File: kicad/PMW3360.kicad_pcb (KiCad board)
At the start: 2 copper layers, 22 x 34 mm, 12 parts, among them J1 Conn_01x07, U1 PMW3360, U2 TCR2EF19

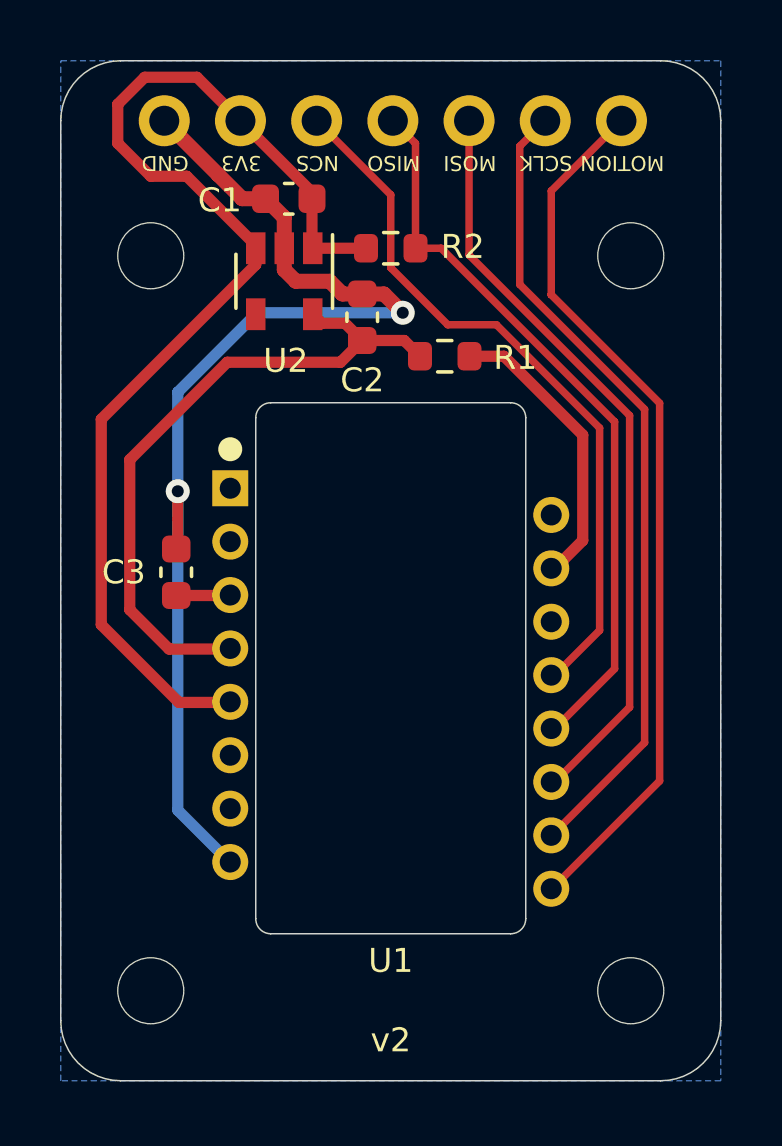
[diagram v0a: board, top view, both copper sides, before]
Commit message: add a reset button
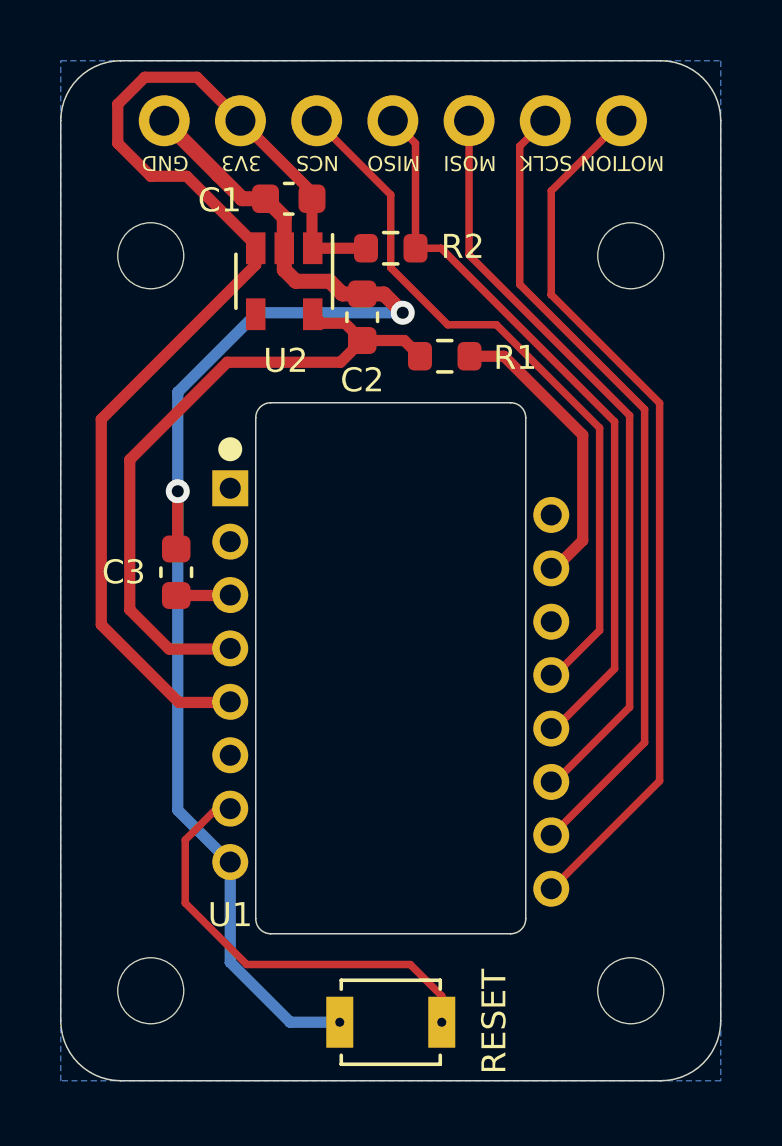
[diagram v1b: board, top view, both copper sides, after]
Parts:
- added sw_reset1: SW_RESET-kbd, mylib:SW_B3U-1000P_reversible, F.Cu at (149.0, 118.0)
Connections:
- U1 pad 1: Net-(U1-Pad1) -> unconnected-(U1-Pad1)
- U1 pad 14: Net-(U1-Pad14) -> unconnected-(U1-Pad14)
- U1 pad 16: Net-(U1-Pad16) -> unconnected-(U1-Pad16)
- U1 pad 2: Net-(U1-Pad2) -> unconnected-(U1-Pad2)
- U1 pad 6: Net-(U1-Pad6) -> unconnected-(U1-Pad6)
- U1 pad 7: Net-(U1-Pad7) -> RESET
- U2 pad 4: Net-(U2-Pad4) -> unconnected-(U2-Pad4)
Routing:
- net RESET: track 0.00 -> 14.7 mm
- net GND: track 38.6 -> 46.3 mm
- net NCS: track 24.5 -> 24.0 mm
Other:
- net class Default removed
- net class power removed
- board text removed: "v2"

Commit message: add 3d model of pmw3360
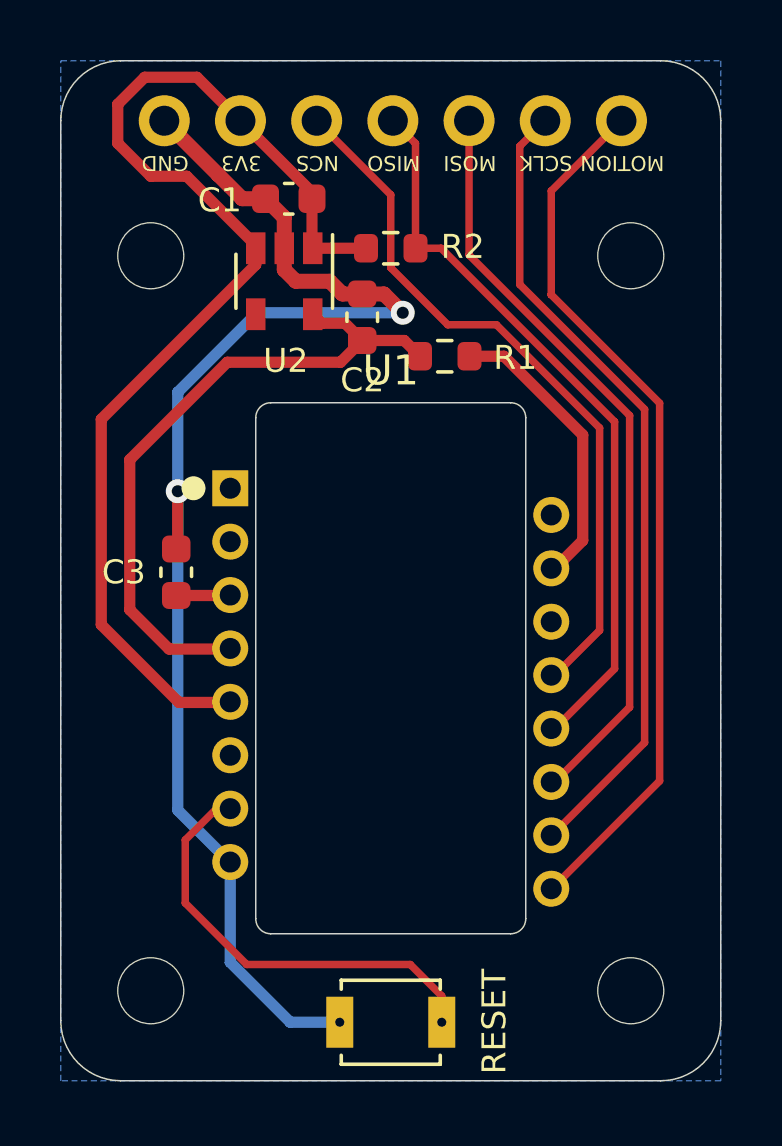
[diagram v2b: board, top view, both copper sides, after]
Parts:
- U1: footprint PMW3360:PMW3360 -> mylib:PMW3360
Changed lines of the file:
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@@
     (pad "" np_thru_hole circle locked (at 0 0) (size 2.2 2.2) (drill 2.2) (layers *.Cu *.Mask))
   )
-  (footprint "PMW3360:PMW3360" (layer "F.Cu")
+  (footprint "mylib:PMW3360" (layer "F.Cu")
     (at 143.65 100.25)
     (property "Sheetfile" "/home/yong/kbd-src/sensors/pmw3360/pmw3360-breakout/kicad/PMW3360.sch")
     (property "Sheetname" "")
     (attr through_hole)
-    (fp_text reference "U1" (at 0 14.225) (layer "F.SilkS")
-      (effects (font (size 0.8 0.8) (thickness 0.15)))
+    (fp_text reference "U1" (at 5.35 -3.925) (layer "F.SilkS")
+      (effects (font (size 1 1) (thickness 0.15)))
     )
     (fp_text value "PMW3360" (at 5.35 13.375) (layer "F.Fab")
       (effects (font (size 1 1) (thickness 0.15)))
     )
-    (fp_circle (center 0 -1.3) (end 0.2 -1.3) (layer "F.SilkS") (width 0.4) (fill none))
+    (fp_circle (center -1.225 0) (end -1.025 0) (layer "F.SilkS") (width 0.4) (fill none))
+    (fp_line (start 9.65 -2.78) (end 9.65 14.48) (layer "Dwgs.User") (width 0.12))
+    (fp_line (start 5.35 4.66) (end 5.35 6.66) (layer "Dwgs.User") (width 0.12))
+    (fp_line (start 1.05 14.48) (end 9.65 14.48) (layer "Dwgs.User") (width 0.12))
+    (fp_line (start 4.35 5.66) (end 6.35 5.66) (layer "Dwgs.User") (width 0.12))
     (fp_line (start 1.05 -2.78) (end 9.65 -2.78) (layer "Dwgs.User") (width 0.12))
-    (fp_line (start 1.05 14.48) (end 9.65 14.48) (layer "Dwgs.User") (width 0.12))
-    (fp_line (start 9.65 -2.78) (end 9.65 14.48) (layer "Dwgs.User") (width 0.12))
-    (fp_line (start 4.35 5.66) (end 6.35 5.66) (layer "Dwgs.User") (width 0.12))
     (fp_line (start 1.05 -2.78) (end 1.05 14.48) (layer "Dwgs.User") (width 0.12))
-    (fp_line (start 5.35 4.66) (end 5.35 6.66) (layer "Dwgs.User") (width 0.12))
+    (fp_line (start 2.975 -5.21) (end 7.725 -5.21) (layer "B.CrtYd") (width 0.05))
     (fp_line (start -4.075 1.84) (end -4.075 8.89) (layer "B.CrtYd") (width 0.05))
-    (fp_line (start 2.975 -5.21) (end 7.725 -5.21) (layer "B.CrtYd") (width 0.05))
     (fp_line (start 14.775 1.84) (end 14.775 8.89) (layer "B.CrtYd") (width 0.05))
     (fp_line (start 2.975 15.94) (end 7.725 15.94) (layer "B.CrtYd") (width 0.05))
+    (fp_arc (start 7.725 -5.21) (mid 12.710103 -3.145103) (end 14.775 1.84) (layer "B.CrtYd") (width 0.05))
     (fp_arc (start 14.775 8.89) (mid 12.710103 13.875103) (end 7.725 15.94) (layer "B.CrtYd") (width 0.05))
+    (fp_arc (start 2.975 15.94) (mid -2.010103 13.875103) (end -4.075 8.89) (layer "B.CrtYd") (width 0.05))
     (fp_arc (start -4.075 1.84) (mid -2.010103 -3.145103) (end 2.975 -5.21) (layer "B.CrtYd") (width 0.05))
-    (fp_arc (start 2.975 15.94) (mid -2.010103 13.875103) (end -4.075 8.89) (layer "B.CrtYd") (width 0.05))
-    (fp_arc (start 7.725 -5.21) (mid 12.710103 -3.145103) (end 14.775 1.84) (layer "B.CrtYd") (width 0.05))
-    (pad "1" thru_hole rect locked (at 0 0) (size 1.2 1.2) (drill 0.7) (layers *.Cu *.Mask)
+    (pad "1" thru_hole rect (at 0 0) (size 1.2 1.2) (drill 0.7) (layers *.Cu *.Mask)
       (net 2 "unconnected-(U1-Pad1)") (pinfunction "NC") (pintype "no_connect"))
-    (pad "2" thru_hole circle locked (at 0 1.78) (size 1.2 1.2) (drill 0.7) (layers *.Cu *.Mask)
+    (pad "2" thru_hole circle (at 0 1.78) (size 1.2 1.2) (drill 0.7) (layers *.Cu *.Mask)
       (net 3 "unconnected-(U1-Pad2)") (pinfunction "NC") (pintype "no_connect"))
-    (pad "3" thru_hole circle locked (at 0 3.56) (size 1.2 1.2) (drill 0.7) (layers *.Cu *.Mask)
+    (pad "3" thru_hole circle (at 0 3.56) (size 1.2 1.2) (drill 0.7) (layers *.Cu *.Mask)
       (net 10 "Net-(C3-Pad1)") (pinfunction "VDDPIX") (pintype "unspecified"))
-    (pad "4" thru_hole circle locked (at 0 5.34) (size 1.2 1.2) (drill 0.7) (layers *.Cu *.Mask)
+    (pad "4" thru_hole circle (at 0 5.34) (size 1.2 1.2) (drill 0.7) (layers *.Cu *.Mask)
       (net 9 "+1V8") (pinfunction "VDD") (pintype "unspecified"))
-    (pad "5" thru_hole circle locked (at 0 7.12) (size 1.2 1.2) (drill 0.7) (layers *.Cu *.Mask)
+    (pad "5" thru_hole circle (at 0 7.12) (size 1.2 1.2) (drill 0.7) (layers *.Cu *.Mask)
       (net 7 "+3V3") (pinfunction "VDDIO") (pintype "unspecified"))
-    (pad "6" thru_hole circle locked (at 0 8.9) (size 1.2 1.2) (drill 0.7) (layers *.Cu *.Mask)
+    (pad "6" thru_hole circle (at 0 8.9) (size 1.2 1.2) (drill 0.7) (layers *.Cu *.Mask)
       (net 4 "unconnected-(U1-Pad6)") (pinfunction "NC") (pintype "no_connect"))
-    (pad "7" thru_hole circle locked (at 0 10.68) (size 1.2 1.2) (drill 0.7) (layers *.Cu *.Mask)
+    (pad "7" thru_hole circle (at 0 10.68) (size 1.2 1.2) (drill 0.7) (layers *.Cu *.Mask)
       (net 1 "RESET") (pinfunction "NRESET") (pintype "unspecified"))
-    (pad "8" thru_hole circle locked (at 0 12.46) (size 1.2 1.2) (drill 0.7) (layers *.Cu *.Mask)
+    (pad "8" thru_hole circle (at 0 12.46) (size 1.2 1.2) (drill 0.7) (layers *.Cu *.Mask)
       (net 8 "GND") (pinfunction "GND") (pintype "unspecified"))
-    (pad "9" thru_hole circle locked (at 10.7 13.35) (size 1.2 1.2) (drill 0.7) (layers *.Cu *.Mask)
+    (pad "9" thru_hole circle (at 10.7 13.35) (size 1.2 1.2) (drill 0.7) (layers *.Cu *.Mask)
       (net 11 "MOTION") (pinfunction "MOTION") (pintype "unspecified"))
-    (pad "10" thru_hole circle locked (at 10.7 11.57) (size 1.2 1.2) (drill 0.7) (layers *.Cu *.Mask)
+    (pad "10" thru_hole circle (at 10.7 11.57) (size 1.2 1.2) (drill 0.7) (layers *.Cu *.Mask)
       (net 12 "SCLK") (pinfunction "SCLK") (pintype "unspecified"))
-    (pad "11" thru_hole circle locked (at 10.7 9.79) (size 1.2 1.2) (drill 0.7) (layers *.Cu *.Mask)
+    (pad "11" thru_hole circle (at 10.7 9.79) (size 1.2 1.2) (drill 0.7) (layers *.Cu *.Mask)
       (net 13 "MOSI") (pinfunction "MOSI") (pintype "unspecified"))
-    (pad "12" thru_hole circle locked (at 10.7 8.01) (size 1.2 1.2) (drill 0.7) (layers *.Cu *.Mask)
+    (pad "12" thru_hole circle (at 10.7 8.01) (size 1.2 1.2) (drill 0.7) (layers *.Cu *.Mask)
       (net 14 "MISO") (pinfunction "MISO") (pintype "unspecified"))
-    (pad "13" thru_hole circle locked (at 10.7 6.23) (size 1.2 1.2) (drill 0.7) (layers *.Cu *.Mask)
+    (pad "13" thru_hole circle (at 10.7 6.23) (size 1.2 1.2) (drill 0.7) (layers *.Cu *.Mask)
       (net 15 "NCS") (pinfunction "NCS") (pintype "unspecified"))
-    (pad "14" thru_hole circle locked (at 10.7 4.45) (size 1.2 1.2) (drill 0.7) (layers *.Cu *.Mask)
+    (pad "14" thru_hole circle (at 10.7 4.45) (size 1.2 1.2) (drill 0.7) (layers *.Cu *.Mask)
       (net 6 "unconnected-(U1-Pad14)") (pinfunction "NC") (pintype "no_connect"))
-    (pad "15" thru_hole circle locked (at 10.7 2.67) (size 1.2 1.2) (drill 0.7) (layers *.Cu *.Mask)
+    (pad "15" thru_hole circle (at 10.7 2.67) (size 1.2 1.2) (drill 0.7) (layers *.Cu *.Mask)
       (net 16 "Net-(R1-Pad2)") (pinfunction "LED_P") (pintype "unspecified"))
-    (pad "16" thru_hole circle locked (at 10.7 0.89) (size 1.2 1.2) (drill 0.7) (layers *.Cu *.Mask)
+    (pad "16" thru_hole circle (at 10.7 0.89) (size 1.2 1.2) (drill 0.7) (layers *.Cu *.Mask)
       (net 5 "unconnected-(U1-Pad16)") (pinfunction "NC") (pintype "no_connect"))
+    (model "${MYLIB_DIR}/3dmodels/peripherals/PMW3360 v12.step"
+      (offset (xyz 5.3 -5.7 2.14))
+      (scale (xyz 1 1 1))
+      (rotate (xyz 0 0 0))
+    )
   )
   (footprint "Capacitor_SMD:C_0603_1608Metric" (layer "F.Cu")
